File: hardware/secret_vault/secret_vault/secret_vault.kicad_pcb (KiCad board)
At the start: 2 copper layers, 121.9 x 55.9 mm, 15 parts, among them J1 Conn_01x04_Female, SW1 SW_Push, SW2 SW_Push, SW3 SW_Push, SW4 SW_Push, SW5 SW_Push, SW6 SW_Push, U1 DS1307N+, Y1 Crystal

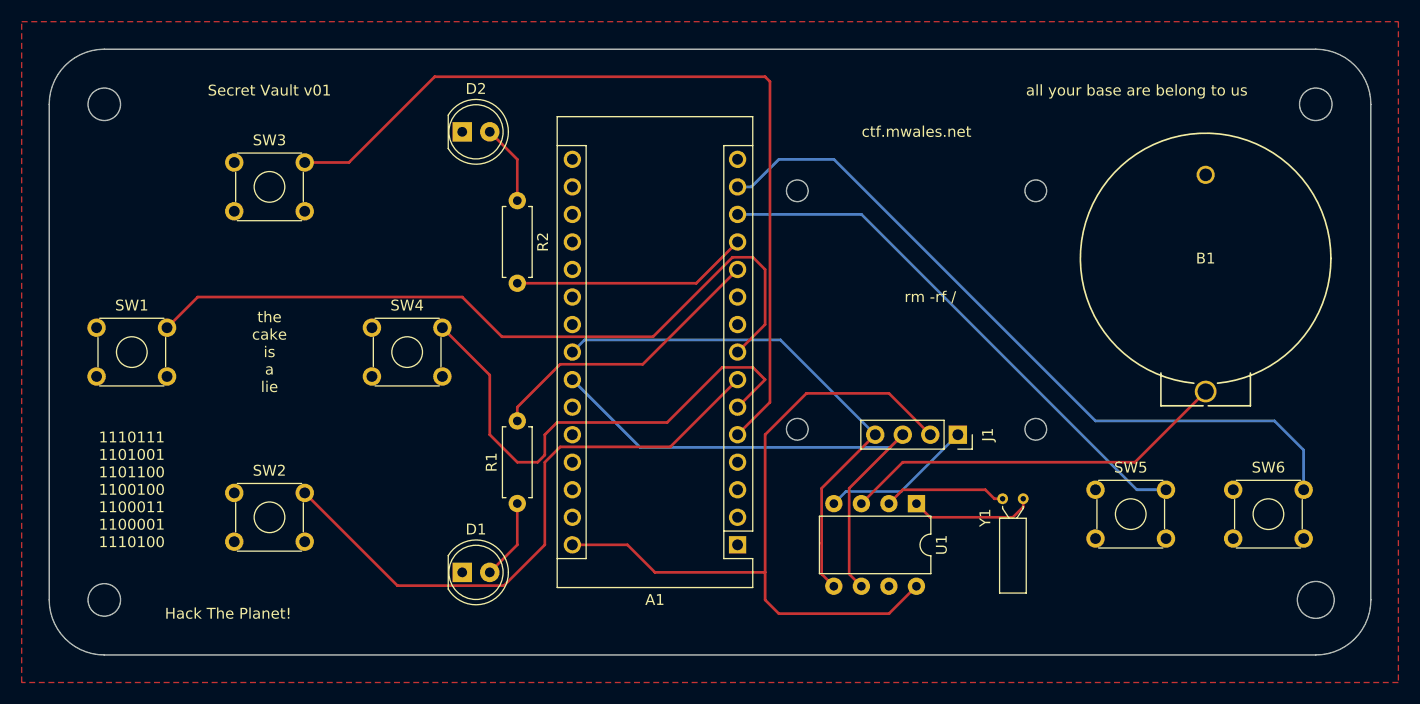
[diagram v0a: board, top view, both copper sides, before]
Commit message: Many fixes to the v0.2 secret vault board
- Added pullup resistor for I2C lines
- All of the switch footprints were wrong
- RTC Vcc tied to 5V instead of Vin
- Added QR code to silkscreen
- Made the resistors a larger part
- Enlarged many of the fonts
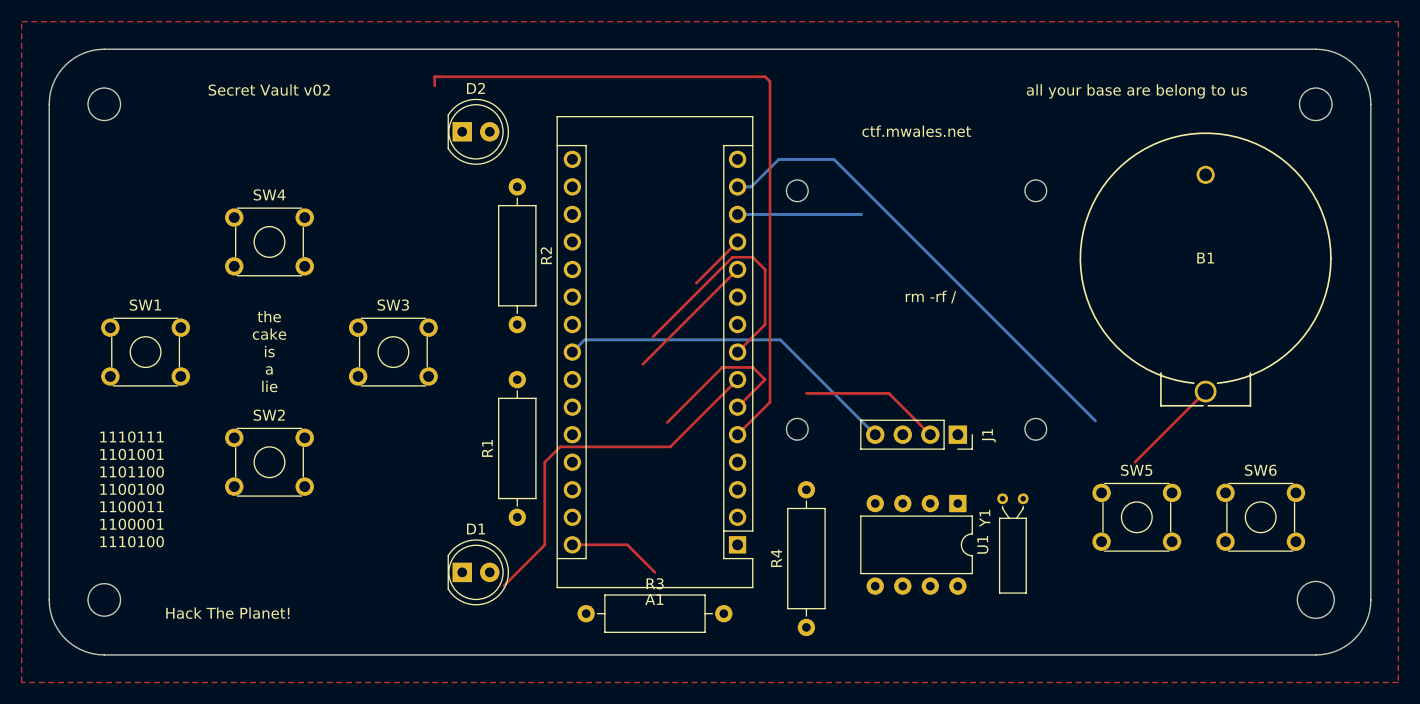
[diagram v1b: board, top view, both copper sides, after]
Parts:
- added R3: 2.2K, Resistor_THT:R_Axial_DIN0309_L9.0mm_D3.2mm_P12.70mm_Horizontal, F.Cu at (110.5, 123.2)
- added R4: 2.2K, Resistor_THT:R_Axial_DIN0309_L9.0mm_D3.2mm_P12.70mm_Horizontal, F.Cu at (130.8, 124.5)
- R1, R2: footprint Resistor_THT:R_Axial_DIN0207_L6.3mm_D2.5mm_P7.62mm_Horizontal -> Resistor_THT:R_Axial_DIN0309_L9.0mm_D3.2mm_P12.70mm_Horizontal
- SW1, SW2, SW3, SW4, SW5, SW6: footprint Button_Switch_THT:SW_TH_Tactile_Omron_B3F-10xx -> cust_sw:SW_TH_Tactile_Omron_B3F-10xx_stackedpninums
- moved SW3 19.1 mm to (89.5, 96.8)
- moved SW4 16.3 mm to (78.0, 86.7)
- moved SW2 5.08 mm to (78.0, 107.0)
- moved U1 3.82 mm to (144.8, 113.0)
- moved R2 1.27 mm to (104.1, 83.8)
- moved R1 1.27 mm to (104.1, 114.3)
- moved SW1 1.27 mm to (66.6, 96.8)
- moved SW6 0.77 mm to (169.5, 112.0)
- moved SW5 0.63 mm to (158.0, 112.0)
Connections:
- A1 pad 27: unconnected-(A1-Pad27) -> OLED_VDD
- A1 pad 30: OLED_VDD -> unconnected-(A1-Pad30)
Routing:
- net OLED_VDD: track 68.0 -> 13.0 mm
- net OLED_SCK: track 50.1 -> 0.00 mm
- net Net-(A1-Pad8): track 70.0 -> 22.5 mm
- net Net-(A1-Pad13): track 50.0 -> 11.4 mm
- net Net-(A1-Pad6): track 46.9 -> 15.2 mm
- net Net-(B1-Pad2): track 36.0 -> 9.22 mm
- net Net-(A1-Pad14): track 68.0 -> 44.1 mm
- net Net-(A1-Pad7): track 55.8 -> 33.9 mm
- net Net-(A1-Pad12): track 21.9 -> 5.39 mm
- net OLED_SDA: track 48.5 -> 32.0 mm
- net Net-(A1-Pad11): track 26.9 -> 12.4 mm
- net Net-(A1-Pad5): track 80.2 -> 65.8 mm
- net OLED_GND: track 14.1 -> 0.00 mm
- net Net-(U1-Pad1): track 11.5 -> 0.00 mm
- net Net-(U1-Pad2): track 11.4 -> 0.00 mm
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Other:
- board text added: "Secret Vault v02"
- board text removed: "Secret Vault v01"

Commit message: Didn't have PCB saved
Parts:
- added G***: LOGO, qr:qrcode2, F.Cu at (141.0, 94.0)
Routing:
- net OLED_VDD: track 13.0 -> 88.7 mm
- net OLED_SCK: track 0.00 -> 61.8 mm
- net Net-(A1-Pad6): track 15.2 -> 65.8 mm
- net Net-(A1-Pad13): track 11.4 -> 57.3 mm
- net OLED_GND: track 0.00 -> 42.3 mm
- net Net-(A1-Pad8): track 22.5 -> 59.8 mm
- net Net-(A1-Pad5): track 65.8 -> 99.9 mm
- net Net-(A1-Pad14): track 44.1 -> 71.1 mm
- net Net-(B1-Pad2): track 9.22 -> 32.2 mm
- net OLED_SDA: track 32.0 -> 52.0 mm
- net Net-(A1-Pad12): track 5.39 -> 24.2 mm
- net Net-(A1-Pad7): track 33.9 -> 50.5 mm
- net Net-(A1-Pad11): track 12.4 -> 24.5 mm
- net Net-(U1-Pad2): track 0.00 -> 9.03 mm
- net Net-(U1-Pad1): track 0.00 -> 8.70 mm
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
